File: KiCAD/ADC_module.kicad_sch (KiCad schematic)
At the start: 5 parts, among them U35 AD7523JN, U36 LM358

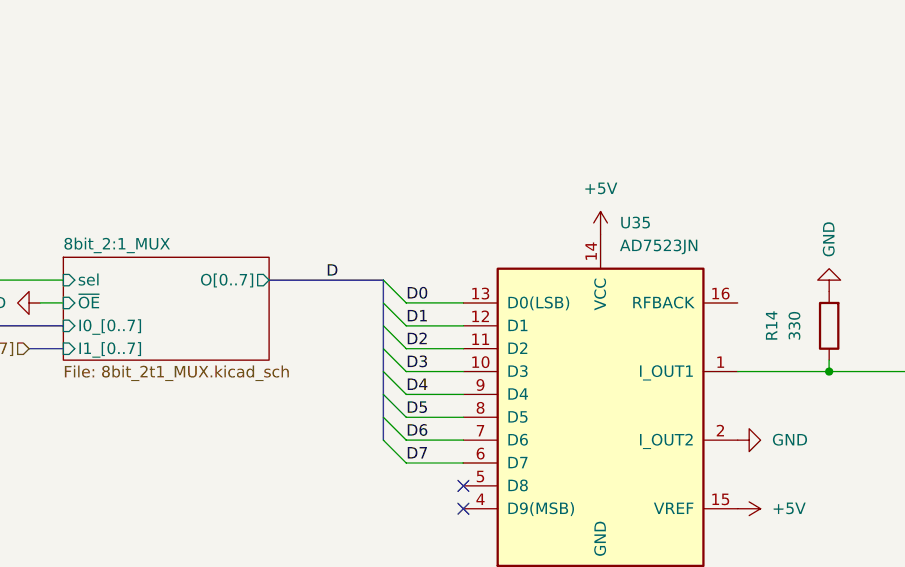
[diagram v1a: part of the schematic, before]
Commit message: fix multiple ERCs that made RAM addrs not connecting
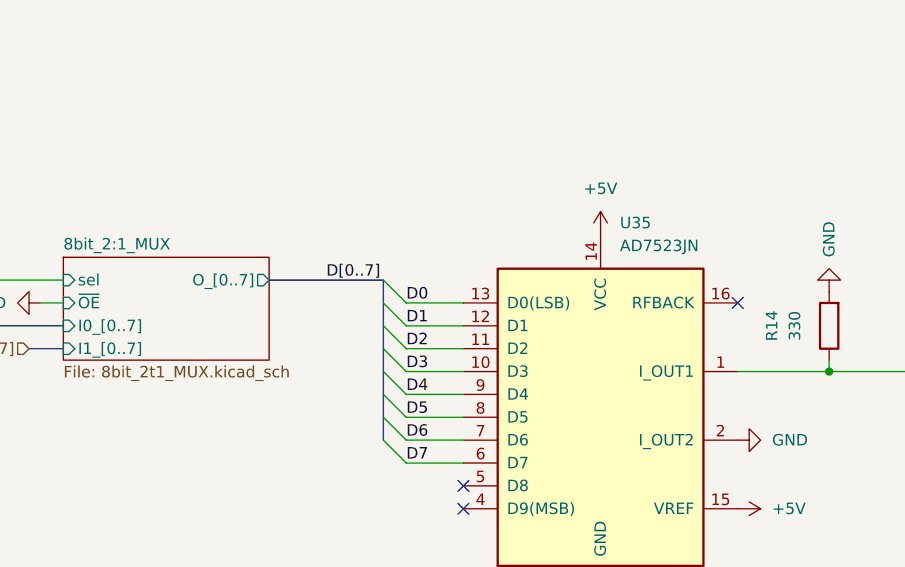
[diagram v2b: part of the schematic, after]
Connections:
- no-connect marks 6 -> 7
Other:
- sheet 8bit_2:1_MUX ports: added O_[0..7]; removed O[0..7]
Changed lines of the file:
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@@
+	)
+	(no_connect
+		(at 140.97 83.82)
 	)
 	(no_connect
@@
 		)
 	)
-	(label "D"
+	(label "D[0..7]"
 		(at 95.25 81.28 0)
 		(effects
@@
 			)
 		)
-		(pin "O[0..7]" output
+		(pin "O_[0..7]" output
 			(at 88.9 81.28 0)
 			(effects

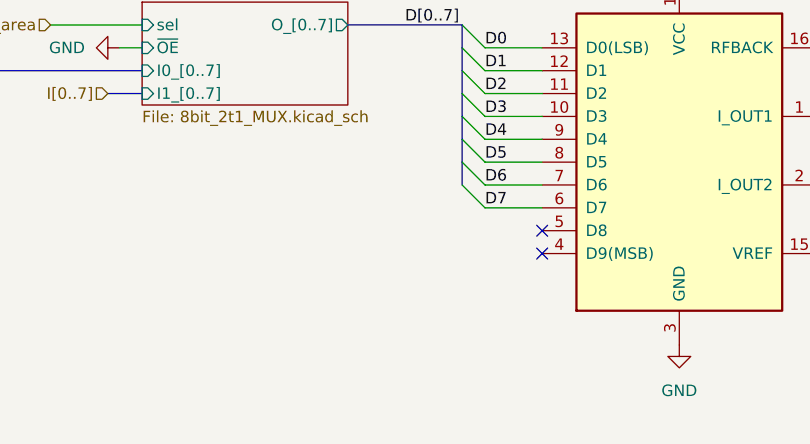
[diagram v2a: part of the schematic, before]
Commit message: add schematics todos for DAC and RAM state controller
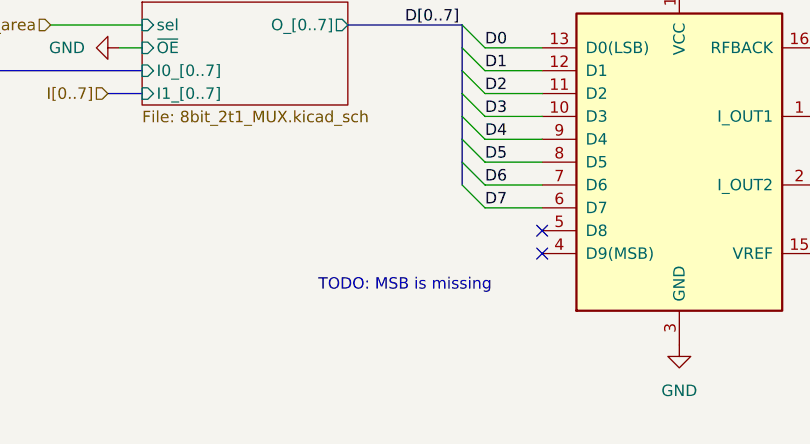
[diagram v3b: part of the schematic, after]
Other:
- note added: "TODO: MSB is missing"
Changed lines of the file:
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@@
 	(generator_version "9.0")
 	(paper "A4")
+	(text "TODO: MSB is missing\n"
+		(exclude_from_sim no)
+		(at 95.25 110.236 0)
+		(effects
+			(font
+				(size 1.27 1.27)
+			)
+		)
+	)
 	(junction
 		(at 182.88 93.98)

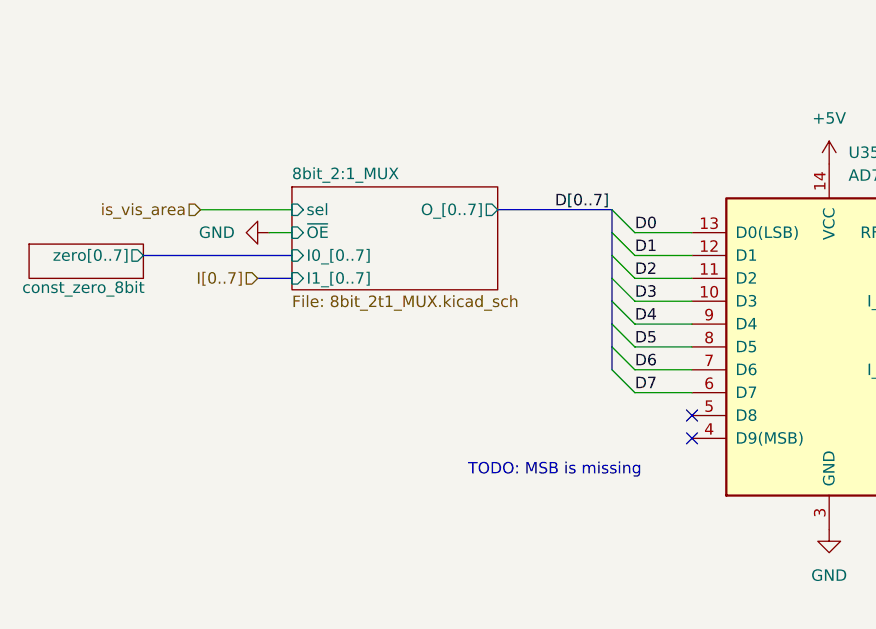
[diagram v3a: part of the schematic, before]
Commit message: update DAC schematics; update pin layout for esp32 connector; update RAM state controller input pin
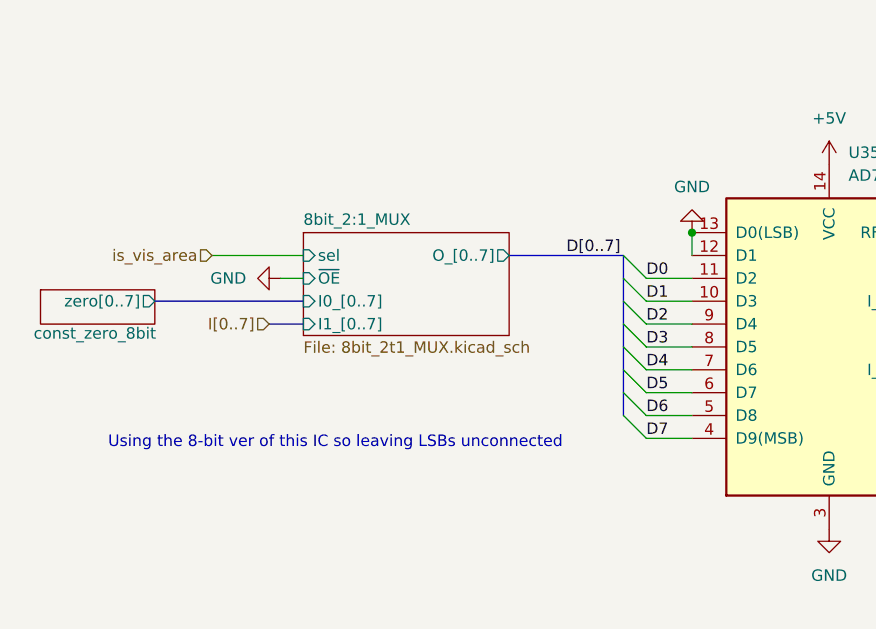
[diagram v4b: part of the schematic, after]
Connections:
- net D0: now also U35.11 (D2); no longer U35.13 (D0(LSB))
- net D1: now also U35.10 (D3); no longer U35.12 (D1)
- net D2: now also U35.9 (D4); no longer U35.11 (D2)
- net D3: now also U35.8 (D5); no longer U35.10 (D3)
- net D4: now also U35.7 (D6); no longer U35.9 (D4)
- net D5: now also U35.6 (D7); no longer U35.8 (D5)
- net D6: now also U35.5 (D8); no longer U35.7 (D6)
- net D7: now also U35.4 (D9(MSB)); no longer U35.6 (D7)
- net GND: now also U35.12 (D1), U35.13 (D0(LSB))
- no-connect marks 7 -> 5
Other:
- note added: "Using the 8-bit ver of this IC so leaving LSBs unconnected"
- note removed: "TODO: MSB is missing"
